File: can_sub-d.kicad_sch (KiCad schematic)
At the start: 5 parts

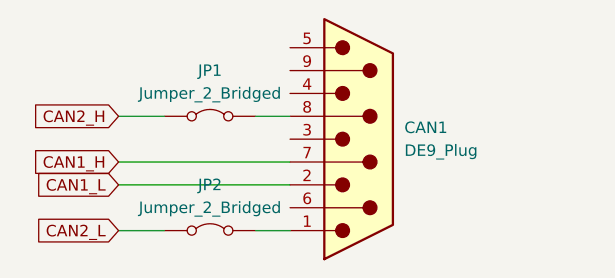
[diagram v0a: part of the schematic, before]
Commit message: rename jumpers
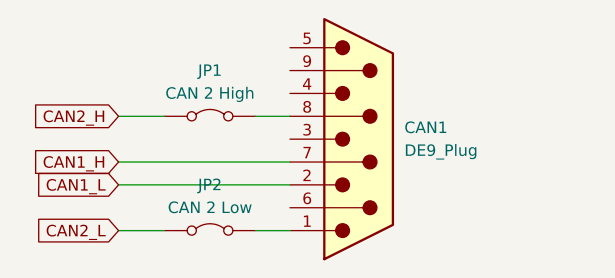
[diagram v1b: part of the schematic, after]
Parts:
- JP1: value Jumper_2_Bridged -> CAN 2 High
- JP2: value Jumper_2_Bridged -> CAN 2 Low
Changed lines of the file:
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@@
 			)
 		)
-		(property "Value" "Jumper_2_Bridged"
+		(property "Value" "CAN 2 Low"
 			(at 58.42 63.5 0)
 			(effects
@@
 			)
 		)
-		(property "Value" "Jumper_2_Bridged"
+		(property "Value" "CAN 2 High"
 			(at 58.42 50.8 0)
 			(effects

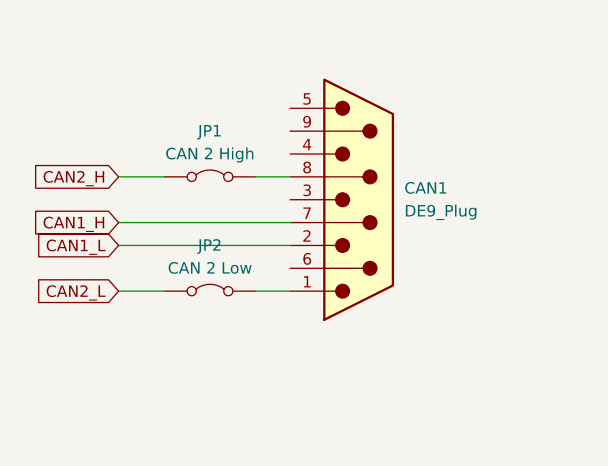
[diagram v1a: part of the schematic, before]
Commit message: adapt Signal net rule
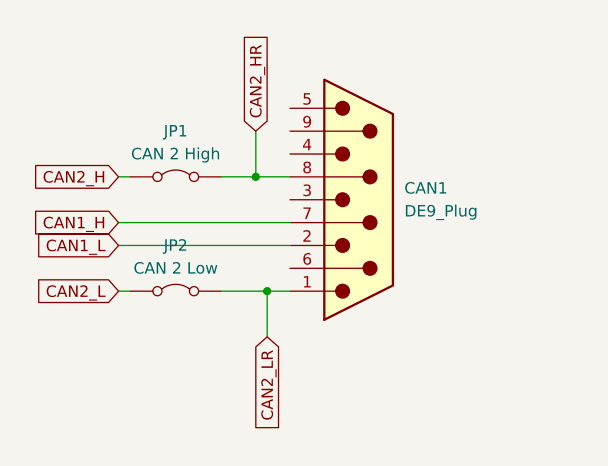
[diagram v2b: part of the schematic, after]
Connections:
- net CAN2_LR: now reaches CAN1.1, JP2.2 (B)
- net CAN2_HR: now reaches CAN1.8, JP1.2 (B)
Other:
- moved on the sheet: JP1, JP2
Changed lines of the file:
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@@
 	(generator_version "8.0")
 	(paper "A4")
-	(wire
-		(pts
-			(xy 63.5 66.04) (xy 67.31 66.04)
-		)
-		(stroke
-			(width 0)
-			(type default)
-		)
-	)
-	(wire
-		(pts
-			(xy 48.26 66.04) (xy 53.34 66.04)
+	(junction
+		(at 64.77 66.04)
+		(diameter 0)
+		(color 0 0 0 0)
+	)
+	(junction
+		(at 63.5 53.34)
+		(diameter 0)
+		(color 0 0 0 0)
+	)
+	(wire
+		(pts
+			(xy 64.77 66.04) (xy 64.77 71.12)
+		)
+		(stroke
+			(width 0)
+			(type default)
+		)
+	)
+	(wire
+		(pts
+			(xy 64.77 66.04) (xy 67.31 66.04)
+		)
+		(stroke
+			(width 0)
+			(type default)
+		)
+	)
+	(wire
+		(pts
+			(xy 63.5 53.34) (xy 67.31 53.34)
+		)
+		(stroke
+			(width 0)
+			(type default)
+		)
+	)
+	(wire
+		(pts
+			(xy 59.69 66.04) (xy 64.77 66.04)
+		)
+		(stroke
+			(width 0)
+			(type default)
+		)
+	)
+	(wire
+		(pts
+			(xy 63.5 48.26) (xy 63.5 53.34)
+		)
+		(stroke
+			(width 0)
+			(type default)
+		)
+	)
+	(wire
+		(pts
+			(xy 48.26 66.04) (xy 49.53 66.04)
 		)
 		(stroke
@@
 	(wire
 		(pts
-			(xy 48.26 53.34) (xy 53.34 53.34)
+			(xy 48.26 53.34) (xy 49.53 53.34)
 		)
 		(stroke
@@
 	(wire
 		(pts
-			(xy 63.5 53.34) (xy 67.31 53.34)
+			(xy 59.69 53.34) (xy 63.5 53.34)
 		)
 		(stroke
@@
 		)
 	)
+	(global_label "CAN2_HR"
+		(shape input)
+		(at 63.5 48.26 90)
+		(fields_autoplaced yes)
+		(effects
+			(font
+				(size 1.27 1.27)
+			)
+			(justify left)
+		)
+		(property "Intersheetrefs" "${INTERSHEET_REFS}"
+			(at 63.5 36.8081 90)
+			(effects
+				(font
+					(size 1.27 1.27)
+				)
+				(justify left)
+				(hide yes)
+			)
+		)
+	)
 	(global_label "CAN2_H"
 		(shape input)
@@
 		(property "Intersheetrefs" "${INTERSHEET_REFS}"
 			(at 38.3805 66.04 0)
+			(effects
+				(font
+					(size 1.27 1.27)
+				)
+				(justify right)
+				(hide yes)
+			)
+		)
+	)
+	(global_label "CAN2_LR"
+		(shape input)
+		(at 64.77 71.12 270)
+		(fields_autoplaced yes)
+		(effects
+			(font
+				(size 1.27 1.27)
+			)
+			(justify right)
+		)
+		(property "Intersheetrefs" "${INTERSHEET_REFS}"
+			(at 64.77 82.2695 90)
 			(effects
 				(font
@@
 	(symbol
 		(lib_id "Jumper:Jumper_2_Bridged")
-		(at 58.42 66.04 0)
+		(at 54.61 66.04 0)
 		(unit 1)
 		(exclude_from_sim yes)
@@
 		(fields_autoplaced yes)
 		(property "Reference" "JP2"
-			(at 58.42 60.96 0)
+			(at 54.61 60.96 0)
 			(effects
 				(font
@@
 		)
 		(property "Value" "CAN 2 Low"
-			(at 58.42 63.5 0)
+			(at 54.61 63.5 0)
 			(effects
 				(font
@@
 		)
 		(property "Footprint" "TestPoint:TestPoint_2Pads_Pitch2.54mm_Drill0.8mm"
-			(at 58.42 66.04 0)
+			(at 54.61 66.04 0)
 			(effects
 				(font
@@
 		)
 		(property "Datasheet" "~"
-			(at 58.42 66.04 0)
+			(at 54.61 66.04 0)
 			(effects
 				(font
@@
 		)
 		(property "Description" "Jumper, 2-pole, closed/bridged"
-			(at 58.42 66.04 0)
+			(at 54.61 66.04 0)
 			(effects
 				(font
@@
 	(symbol
 		(lib_id "Jumper:Jumper_2_Bridged")
-		(at 58.42 53.34 0)
+		(at 54.61 53.34 0)
 		(unit 1)
 		(exclude_from_sim yes)
@@
 		(fields_autoplaced yes)
 		(property "Reference" "JP1"
-			(at 58.42 48.26 0)
+			(at 54.61 48.26 0)
 			(effects
 				(font
@@
 		)
 		(property "Value" "CAN 2 High"
-			(at 58.42 50.8 0)
+			(at 54.61 50.8 0)
 			(effects
 				(font
@@
 		)
 		(property "Footprint" "TestPoint:TestPoint_2Pads_Pitch2.54mm_Drill0.8mm"
-			(at 58.42 53.34 0)
+			(at 54.61 53.34 0)
 			(effects
 				(font
@@
 		)
 		(property "Datasheet" "~"
-			(at 58.42 53.34 0)
+			(at 54.61 53.34 0)
 			(effects
 				(font
@@
 		)
 		(property "Description" "Jumper, 2-pole, closed/bridged"
-			(at 58.42 53.34 0)
-			(effects
-				(font
+			(at 54.61 53.34 0)
+			(effects
+				(font
